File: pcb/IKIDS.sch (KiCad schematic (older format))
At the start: 25 parts, among them U1 Elite-C

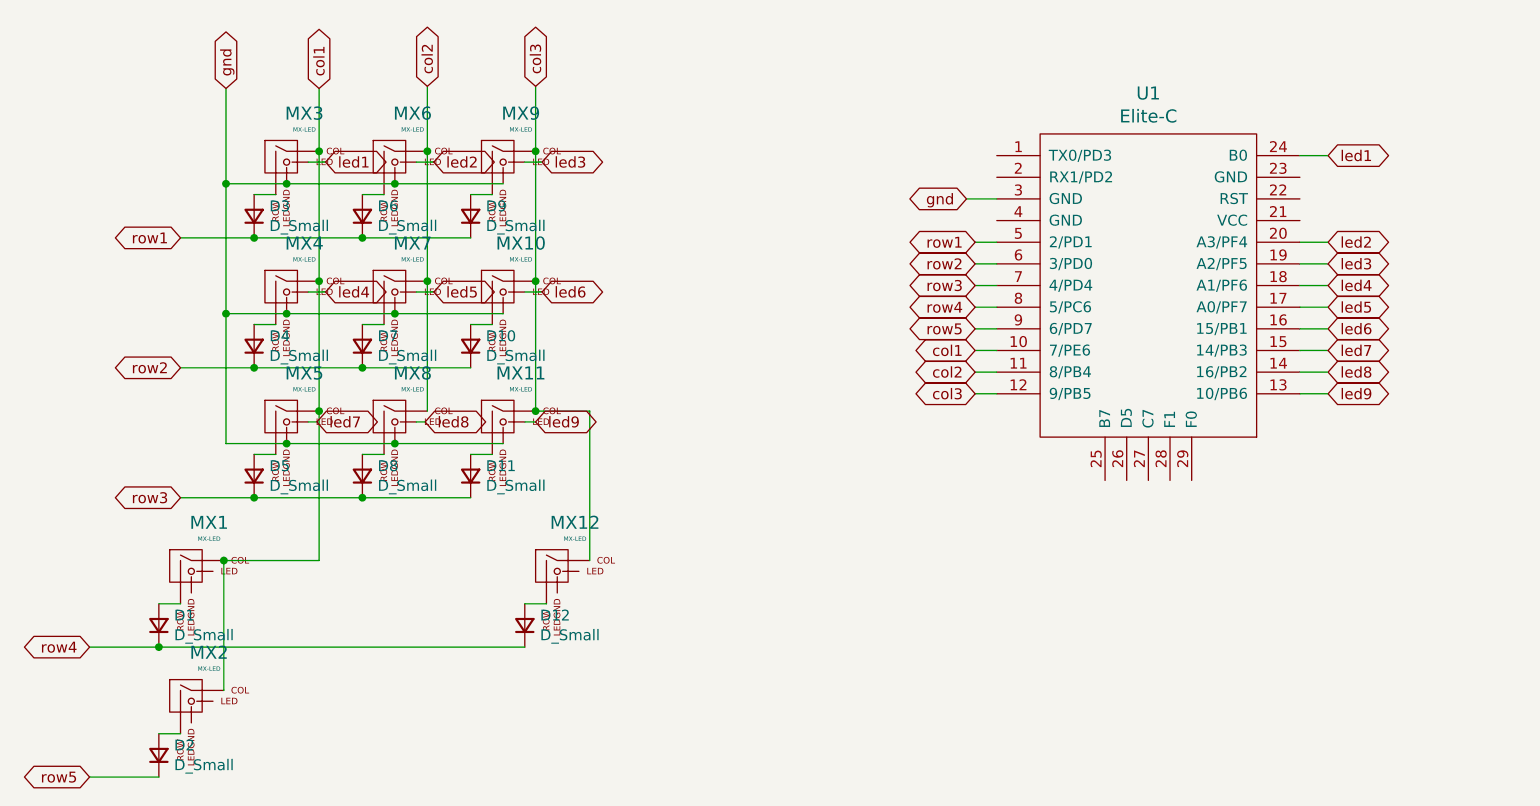
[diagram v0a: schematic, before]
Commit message: hooked up bottom 3 LEDS
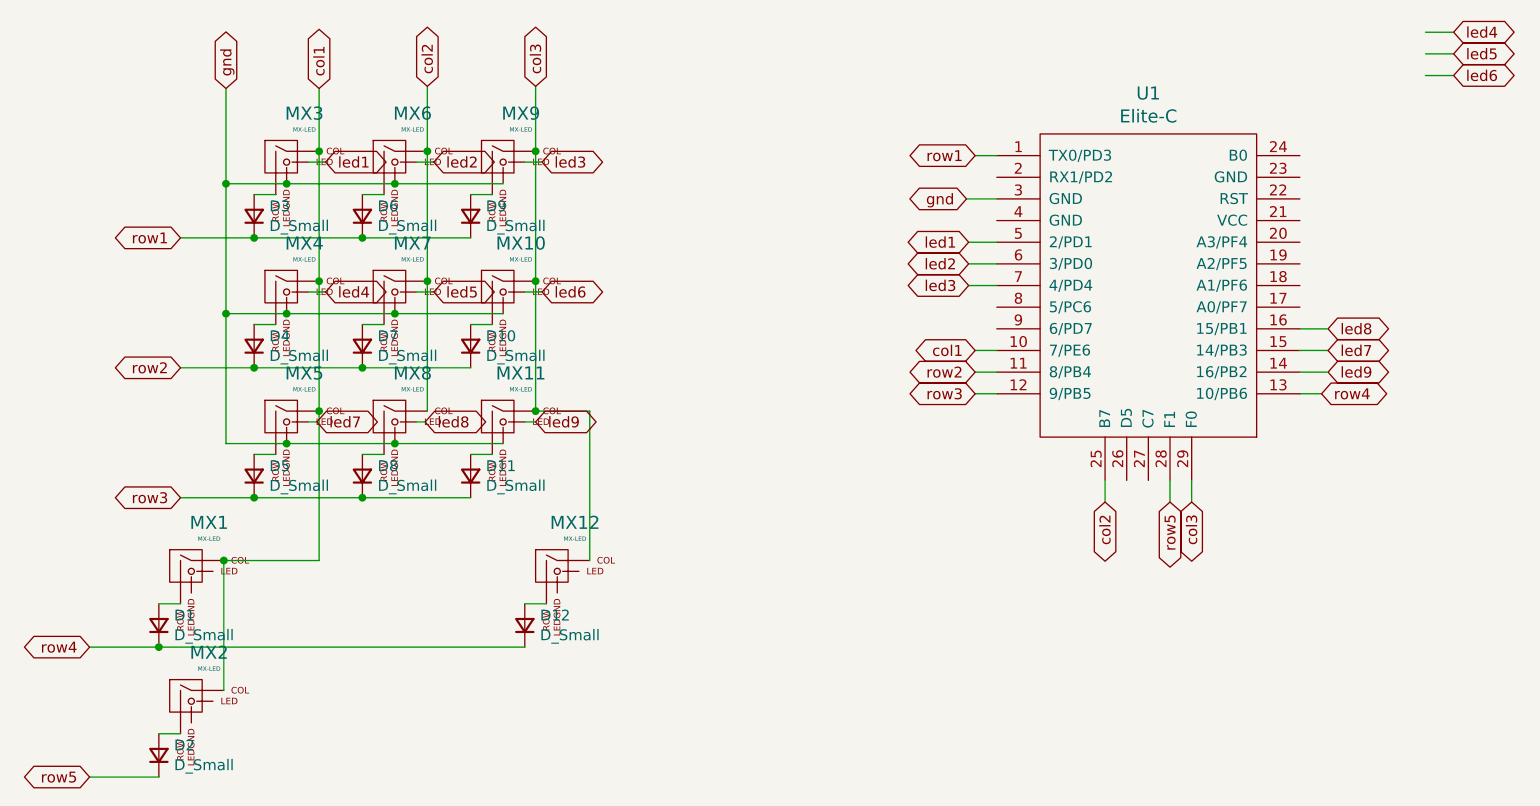
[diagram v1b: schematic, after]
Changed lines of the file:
@@
 	1    0    0    -1
 $EndComp
-Text GLabel 8730 2900 0    50   BiDi ~ 0
+Text GLabel 8730 2500 0    50   BiDi ~ 0
 row1
 Wire Wire Line
-	8730 2900 8830 2900
-Text GLabel 8730 3000 0    50   BiDi ~ 0
+	8730 2500 8830 2500
+Text GLabel 8730 3500 0    50   BiDi ~ 0
 row2
 Wire Wire Line
-	8730 3000 8830 3000
-Text GLabel 8730 3100 0    50   BiDi ~ 0
-row3
-Wire Wire Line
-	8730 3100 8830 3100
-Text GLabel 8730 3200 0    50   BiDi ~ 0
+	8730 3500 8830 3500
+Text GLabel 10330 3600 2    50   BiDi ~ 0
 row4
 Wire Wire Line
-	8730 3200 8830 3200
-Text GLabel 8730 3300 0    50   BiDi ~ 0
+	10330 3600 10230 3600
+Text GLabel 9630 4100 3    50   BiDi ~ 0
 row5
 Wire Wire Line
-	8730 3300 8830 3300
+	9630 4100 9630 4000
 Text GLabel 8730 3400 0    50   BiDi ~ 0
 col1
-Text GLabel 8730 3500 0    50   BiDi ~ 0
+Text GLabel 9330 4100 3    50   BiDi ~ 0
 col2
-Text GLabel 8730 3600 0    50   BiDi ~ 0
+Text GLabel 9730 4100 3    50   BiDi ~ 0
 col3
 Wire Wire Line
-	8730 3600 8830 3600
-Wire Wire Line
-	8830 3500 8730 3500
+	9730 4100 9730 4000
+Wire Wire Line
+	9330 4000 9330 4100
 Wire Wire Line
 	8730 3400 8830 3400
@@
 Wire Wire Line
 	6650 2530 6730 2530
-Text GLabel 10360 2500 2    50   BiDi ~ 0
+Text GLabel 8700 2900 0    50   BiDi ~ 0
 led1
-Text GLabel 10360 2900 2    50   BiDi ~ 0
+Text GLabel 8700 3000 0    50   BiDi ~ 0
 led2
-Text GLabel 10360 3000 2    50   BiDi ~ 0
+Text GLabel 8700 3100 0    50   BiDi ~ 0
 led3
-Text GLabel 10360 3100 2    50   BiDi ~ 0
-led4
-Text GLabel 10360 3200 2    50   BiDi ~ 0
-led5
-Text GLabel 10360 3300 2    50   BiDi ~ 0
-led6
 Text GLabel 10360 3400 2    50   BiDi ~ 0
 led7
 Text GLabel 10360 3500 2    50   BiDi ~ 0
+led9
+Wire Wire Line
+	10360 3500 10230 3500
+Wire Wire Line
+	10360 3400 10230 3400
+Wire Wire Line
+	10940 2030 10810 2030
+Wire Wire Line
+	10810 1930 10940 1930
+Wire Wire Line
+	8700 3100 8830 3100
+Wire Wire Line
+	8700 3000 8830 3000
+Wire Wire Line
+	8830 2900 8700 2900
+Wire Wire Line
+	8730 3600 8830 3600
+Text GLabel 8730 3600 0    50   BiDi ~ 0
+row3
+Wire Wire Line
+	10810 2130 10940 2130
+Wire Wire Line
+	10230 3300 10360 3300
+Text GLabel 10360 3300 2    50   BiDi ~ 0
 led8
-Text GLabel 10360 3600 2    50   BiDi ~ 0
-led9
-Wire Wire Line
-	10360 3600 10230 3600
-Wire Wire Line
-	10230 3500 10360 3500
-Wire Wire Line
-	10360 3400 10230 3400
-Wire Wire Line
-	10230 3300 10360 3300
-Wire Wire Line
-	10360 3200 10230 3200
-Wire Wire Line
-	10230 3100 10360 3100
-Wire Wire Line
-	10360 3000 10230 3000
-Wire Wire Line
-	10360 2900 10230 2900
-Wire Wire Line
-	10230 2500 10360 2500
+Text GLabel 10940 2130 2    50   BiDi ~ 0
+led6
+Text GLabel 10940 2030 2    50   BiDi ~ 0
+led5
+Text GLabel 10940 1930 2    50   BiDi ~ 0
+led4
 $EndSCHEMATC

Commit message: updated diode footprint to D_SOD-123
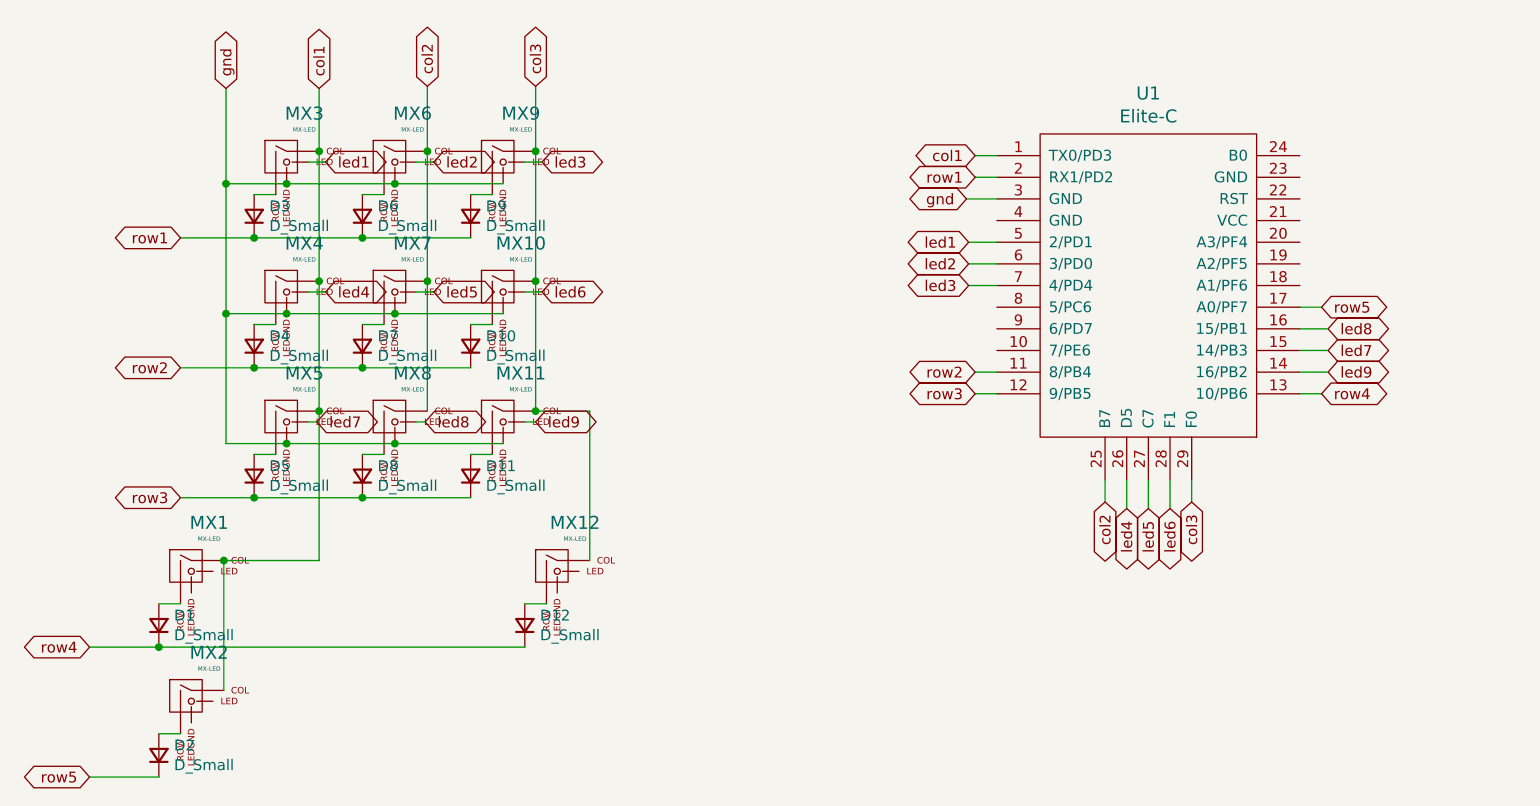
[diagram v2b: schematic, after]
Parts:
- D1, D10, D11, D12, D2, D3, D4, D5, D6, D7, D8, D9: footprint Diode_SMD:D_0805_2012Metric -> Diode_SMD:D_SOD-123
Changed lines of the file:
@@
 	1    0    0    -1
 $EndComp
-Text GLabel 8730 2500 0    50   BiDi ~ 0
+Text GLabel 8730 2600 0    50   BiDi ~ 0
 row1
 Wire Wire Line
-	8730 2500 8830 2500
+	8730 2600 8830 2600
 Text GLabel 8730 3500 0    50   BiDi ~ 0
 row2
@@
 Wire Wire Line
 	10330 3600 10230 3600
-Text GLabel 9630 4100 3    50   BiDi ~ 0
+Text GLabel 10330 3200 2    50   BiDi ~ 0
 row5
 Wire Wire Line
-	9630 4100 9630 4000
-Text GLabel 8730 3400 0    50   BiDi ~ 0
+	10330 3200 10230 3200
+Text GLabel 8730 2500 0    50   BiDi ~ 0
 col1
 Text GLabel 9330 4100 3    50   BiDi ~ 0
@@
 	9330 4000 9330 4100
 Wire Wire Line
-	8730 3400 8830 3400
+	8730 2500 8830 2500
 $Comp
 L MX_Alps_Hybrid:MX-LED MX3
@@
 F 0 "D3" V 5446 2710 50  0000 R CNN
 F 1 "D_Small" V 5355 2710 50  0000 R CNN
-F 2 "Diode_SMD:D_0805_2012Metric" V 5400 2780 50  0001 C CNN
+F 2 "Diode_SMD:D_SOD-123" V 5400 2780 50  0001 C CNN
 F 3 "~" V 5400 2780 50  0001 C CNN
 	1    5400 2780
@@
 F 0 "D6" V 5946 2710 50  0000 R CNN
 F 1 "D_Small" V 5855 2710 50  0000 R CNN
-F 2 "Diode_SMD:D_0805_2012Metric" V 5900 2780 50  0001 C CNN
+F 2 "Diode_SMD:D_SOD-123" V 5900 2780 50  0001 C CNN
 F 3 "~" V 5900 2780 50  0001 C CNN
 	1    5900 2780
@@
 F 0 "D9" V 6446 2710 50  0000 R CNN
 F 1 "D_Small" V 6355 2710 50  0000 R CNN
-F 2 "Diode_SMD:D_0805_2012Metric" V 6400 2780 50  0001 C CNN
+F 2 "Diode_SMD:D_SOD-123" V 6400 2780 50  0001 C CNN
 F 3 "~" V 6400 2780 50  0001 C CNN
 	1    6400 2780
@@
 F 0 "D4" V 5446 3310 50  0000 R CNN
 F 1 "D_Small" V 5355 3310 50  0000 R CNN
-F 2 "Diode_SMD:D_0805_2012Metric" V 5400 3380 50  0001 C CNN
+F 2 "Diode_SMD:D_SOD-123" V 5400 3380 50  0001 C CNN
 F 3 "~" V 5400 3380 50  0001 C CNN
 	1    5400 3380
@@
 F 0 "D7" V 5946 3310 50  0000 R CNN
 F 1 "D_Small" V 5855 3310 50  0000 R CNN
-F 2 "Diode_SMD:D_0805_2012Metric" V 5900 3380 50  0001 C CNN
+F 2 "Diode_SMD:D_SOD-123" V 5900 3380 50  0001 C CNN
 F 3 "~" V 5900 3380 50  0001 C CNN
 	1    5900 3380
@@
 F 0 "D10" V 6446 3310 50  0000 R CNN
 F 1 "D_Small" V 6355 3310 50  0000 R CNN
-F 2 "Diode_SMD:D_0805_2012Metric" V 6400 3380 50  0001 C CNN
+F 2 "Diode_SMD:D_SOD-123" V 6400 3380 50  0001 C CNN
 F 3 "~" V 6400 3380 50  0001 C CNN
 	1    6400 3380
@@
 F 0 "D5" V 5446 3910 50  0000 R CNN
 F 1 "D_Small" V 5355 3910 50  0000 R CNN
-F 2 "Diode_SMD:D_0805_2012Metric" V 5400 3980 50  0001 C CNN
+F 2 "Diode_SMD:D_SOD-123" V 5400 3980 50  0001 C CNN
 F 3 "~" V 5400 3980 50  0001 C CNN
 	1    5400 3980
@@
 F 0 "D8" V 5946 3910 50  0000 R CNN
 F 1 "D_Small" V 5855 3910 50  0000 R CNN
-F 2 "Diode_SMD:D_0805_2012Metric" V 5900 3980 50  0001 C CNN
+F 2 "Diode_SMD:D_SOD-123" V 5900 3980 50  0001 C CNN
 F 3 "~" V 5900 3980 50  0001 C CNN
 	1    5900 3980
@@
 F 0 "D11" V 6446 3910 50  0000 R CNN
 F 1 "D_Small" V 6355 3910 50  0000 R CNN
-F 2 "Diode_SMD:D_0805_2012Metric" V 6400 3980 50  0001 C CNN
+F 2 "Diode_SMD:D_SOD-123" V 6400 3980 50  0001 C CNN
 F 3 "~" V 6400 3980 50  0001 C CNN
 	1    6400 3980
@@
 F 0 "D1" V 5006 4600 50  0000 R CNN
 F 1 "D_Small" V 4915 4600 50  0000 R CNN
-F 2 "Diode_SMD:D_0805_2012Metric" V 4960 4670 50  0001 C CNN
+F 2 "Diode_SMD:D_SOD-123" V 4960 4670 50  0001 C CNN
 F 3 "~" V 4960 4670 50  0001 C CNN
 	1    4960 4670
@@
 F 0 "D2" V 5006 5200 50  0000 R CNN
 F 1 "D_Small" V 4915 5200 50  0000 R CNN
-F 2 "Diode_SMD:D_0805_2012Metric" V 4960 5270 50  0001 C CNN
+F 2 "Diode_SMD:D_SOD-123" V 4960 5270 50  0001 C CNN
 F 3 "~" V 4960 5270 50  0001 C CNN
 	1    4960 5270
@@
 F 0 "D12" V 6696 4600 50  0000 R CNN
 F 1 "D_Small" V 6605 4600 50  0000 R CNN
-F 2 "Diode_SMD:D_0805_2012Metric" V 6650 4670 50  0001 C CNN
+F 2 "Diode_SMD:D_SOD-123" V 6650 4670 50  0001 C CNN
 F 3 "~" V 6650 4670 50  0001 C CNN
 	1    6650 4670
@@
 	10360 3400 10230 3400
 Wire Wire Line
-	10940 2030 10810 2030
-Wire Wire Line
-	10810 1930 10940 1930
+	9530 4130 9530 4000
+Wire Wire Line
+	9430 4000 9430 4130
 Wire Wire Line
 	8700 3100 8830 3100
@@
 row3
 Wire Wire Line
-	10810 2130 10940 2130
+	9630 4000 9630 4130
 Wire Wire Line
 	10230 3300 10360 3300
 Text GLabel 10360 3300 2    50   BiDi ~ 0
 led8
-Text GLabel 10940 2130 2    50   BiDi ~ 0
+Text GLabel 9630 4130 3    50   BiDi ~ 0
 led6
-Text GLabel 10940 2030 2    50   BiDi ~ 0
+Text GLabel 9530 4130 3    50   BiDi ~ 0
 led5
-Text GLabel 10940 1930 2    50   BiDi ~ 0
+Text GLabel 9430 4130 3    50   BiDi ~ 0
 led4
 $EndSCHEMATC

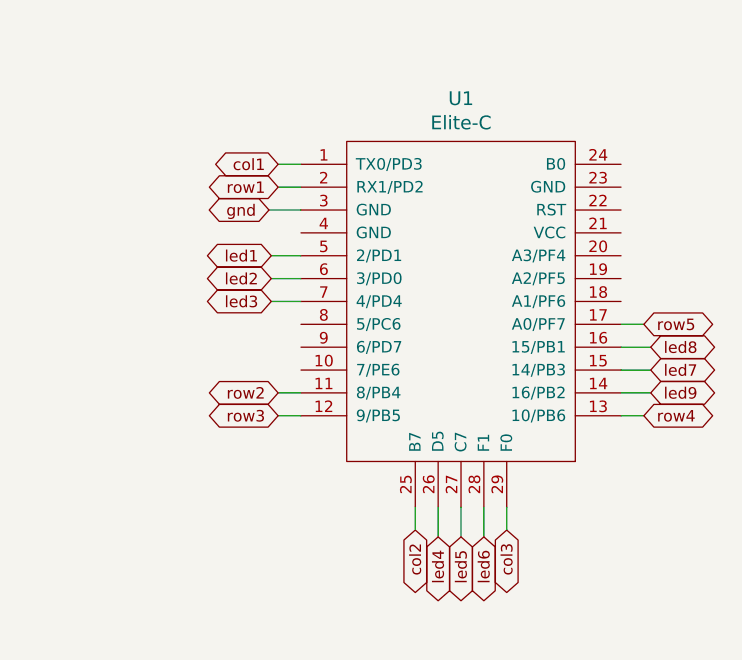
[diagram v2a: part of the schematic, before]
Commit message: Flipped Elite-c for easier case making.
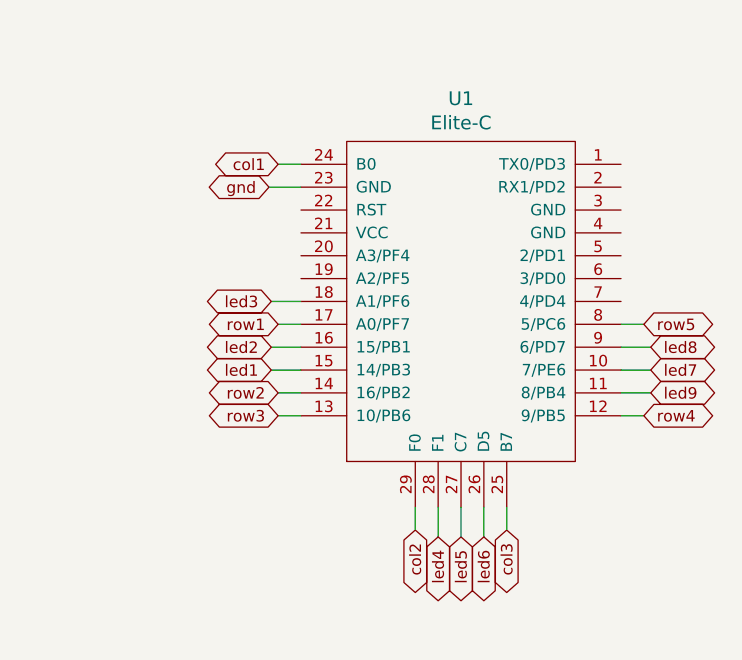
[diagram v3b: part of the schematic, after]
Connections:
- net col1: now also U1.24 (B0); no longer U1.1 (TX0/PD3)
- net col2: now also U1.29 (F0); no longer U1.25 (B7)
- net col3: now also U1.25 (B7); no longer U1.29 (F0)
- net gnd: now also U1.23 (GND); no longer U1.3 (GND)
- net led1: now also U1.15 (14/PB3); no longer U1.5 (2/PD1)
- net led2: now also U1.16 (15/PB1); no longer U1.6 (3/PD0)
- net led3: now also U1.18 (A1/PF6); no longer U1.7 (4/PD4)
- net led4: now also U1.28 (F1); no longer U1.26 (D5)
- net led6: now also U1.26 (D5); no longer U1.28 (F1)
- net led7: now also U1.10 (7/PE6); no longer U1.15 (14/PB3)
- net led8: now also U1.9 (6/PD7); no longer U1.16 (15/PB1)
- net led9: now also U1.11 (8/PB4); no longer U1.14 (16/PB2)
- net row1: now also U1.17 (A0/PF7); no longer U1.2 (RX1/PD2)
- net row2: now also U1.14 (16/PB2); no longer U1.11 (8/PB4)
- net row3: now also U1.13 (10/PB6); no longer U1.12 (9/PB5)
- net row4: now also U1.12 (9/PB5); no longer U1.13 (10/PB6)
- net row5: now also U1.8 (5/PC6); no longer U1.17 (A0/PF7)
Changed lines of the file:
@@
 F 3 "" V 10580 550 60  0001 C CNN
 	1    9530 3050
-	1    0    0    -1
-$EndComp
-Text GLabel 8730 2600 0    50   BiDi ~ 0
-row1
-Wire Wire Line
-	8730 2600 8830 2600
+	-1   0    0    -1
+$EndComp
+Wire Wire Line
+	8730 3200 8830 3200
 Text GLabel 8730 3500 0    50   BiDi ~ 0
 row2
@@
 Text GLabel 5270 2190 1    50   BiDi ~ 0
 gnd
-Text GLabel 8690 2700 0    50   BiDi ~ 0
+Text GLabel 8690 2600 0    50   BiDi ~ 0
 gnd
 Wire Wire Line
-	8690 2700 8830 2700
+	8690 2600 8830 2600
 Text GLabel 5730 2530 2    50   BiDi ~ 0
 led1
@@
 Wire Wire Line
 	6650 2530 6730 2530
-Text GLabel 8700 2900 0    50   BiDi ~ 0
+Text GLabel 8700 3400 0    50   BiDi ~ 0
 led1
-Text GLabel 8700 3000 0    50   BiDi ~ 0
+Text GLabel 8700 3300 0    50   BiDi ~ 0
 led2
 Text GLabel 8700 3100 0    50   BiDi ~ 0
@@
 	8700 3100 8830 3100
 Wire Wire Line
-	8700 3000 8830 3000
-Wire Wire Line
-	8830 2900 8700 2900
+	8700 3300 8830 3300
+Wire Wire Line
+	8830 3400 8700 3400
 Wire Wire Line
 	8730 3600 8830 3600
@@
 Text GLabel 9430 4130 3    50   BiDi ~ 0
 led4
+Text GLabel 8730 3200 0    50   BiDi ~ 0
+row1
 $EndSCHEMATC
